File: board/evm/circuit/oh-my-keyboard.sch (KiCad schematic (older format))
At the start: 0 parts

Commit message: evm sch design finished
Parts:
- added P?: CONN_02X12, symbol CONN_02X12
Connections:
- net labels added: +12V, +3.3V, BAT_BST_EN, BAT_DSEL, BAT_IRQ, BAT_OTG_EN, BAT_SCL, BAT_SDA, BAT_nCE, BLE_SCL, BLE_SDA, CDE, CD_SCL, CD_SDA, CHARGEOE, COB1, COB2, DEV_D+, DEV_D-, FSMC_A0, FSMC_A1, FSMC_A2, FSMC_A3, FSMC_A4, FSMC_A5, FSMC_A6, FSMC_A7, FSMC_D0, FSMC_D1, FSMC_D10, FSMC_D11, FSMC_D12, FSMC_D13, FSMC_D14, FSMC_D15, FSMC_D2, FSMC_D3, FSMC_D4, FSMC_D5, FSMC_D6, FSMC_D7, FSMC_D8, FSMC_D9, FSMC_IRQ, FSMC_OE, FSMC_WE, FSMC_nCS, GND, HOST_D+, HOST_D-, LED_Sihft_CLK0, LED_Storage_CLK0, LED_nCLR, LED_nOE, ScanMatrix0, ScanMatrix1, ScanMatrix10, ScanMatrix11, ScanMatrix12, ScanMatrix13, ScanMatrix14, ScanMatrix15, ScanMatrix16, ScanMatrix17, ScanMatrix18, ScanMatrix19, ScanMatrix2, ScanMatrix20, ScanMatrix21, ScanMatrix22, ScanMatrix23, ScanMatrix3, ScanMatrix4, ScanMatrix5, ScanMatrix6, ScanMatrix7, ScanMatrix8, ScanMatrix9, TOUCH_IRQ, TOUCH_SCK, TOUCH_SDA, nRF24_IRQ
- wire segments 0 -> 239
- no-connect marks 0 -> 7

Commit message: add light sensor
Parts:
- added R?: Photores, symbol Photores
- added R?: R62K, symbol R
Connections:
- wire segments 239 -> 245
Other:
- note added: "FIXME: Double check photo resister's light/dark Rval"
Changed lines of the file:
@@
 F64 "GPIO9" I R 6100 6250 60
 F65 "GPIO10" I R 6100 6350 60
+F66 "ADC_IN" I R 6100 6450 60
 $EndSheet
 Wire Wire Line
@@
 Text Label 6200 6050 0    60   ~ 0
 CDE
+$Comp
+L Photores R?
+U 1 1 575DF76C
+P 7800 6900
+F 0 "R?" V 7880 6900 50  0000 C CNN
+F 1 "Photores" V 8010 6900 50  0000 C TNN
+F 2 "" V 7730 6900 50  0000 C CNN
+F 3 "" H 7800 6900 50  0000 C CNN
+	1    7800 6900
+	1    0    0    -1
+$EndComp
+$Comp
+L +3.3V #PWR?
+U 1 1 575E1819
+P 8350 6400
+F 0 "#PWR?" H 8350 6250 50  0001 C CNN
+F 1 "+3.3V" H 8350 6540 50  0000 C CNN
+F 2 "" H 8350 6400 50  0000 C CNN
+F 3 "" H 8350 6400 50  0000 C CNN
+	1    8350 6400
+	1    0    0    -1
+$EndComp
+$Comp
+L R R?
+U 1 1 575E386A
+P 8050 6450
+F 0 "R?" V 8130 6450 50  0000 C CNN
+F 1 "R62K" V 8050 6450 50  0000 C CNN
+F 2 "" V 7980 6450 50  0000 C CNN
+F 3 "" H 8050 6450 50  0000 C CNN
+	1    8050 6450
+	0    1    1    0
+$EndComp
+Wire Wire Line
+	7800 6650 7800 6450
+Wire Wire Line
+	7800 6450 7900 6450
+Wire Wire Line
+	8200 6450 8350 6450
+Wire Wire Line
+	8350 6450 8350 6400
+$Comp
+L GND #PWR?
+U 1 1 575E448B
+P 7800 7250
+F 0 "#PWR?" H 7800 7000 50  0001 C CNN
+F 1 "GND" H 7800 7100 50  0000 C CNN
+F 2 "" H 7800 7250 50  0000 C CNN
+F 3 "" H 7800 7250 50  0000 C CNN
+	1    7800 7250
+	1    0    0    -1
+$EndComp
+Wire Wire Line
+	7800 7250 7800 7150
+Wire Wire Line
+	6100 6450 7800 6450
+Connection ~ 7800 6450
+Text Notes 8200 6700 0    60   ~ 0
+FIXME: Double check photo resister's light/dark Rval
 $EndSCHEMATC

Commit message: bug fix
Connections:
- net labels added: LED_DATA, LED_Sihft_CLK, LED_Storage_CLK
- net labels removed: LED_Sihft_CLK0, LED_Storage_CLK0
- wire segments 245 -> 247
- no-connect marks 7 -> 6

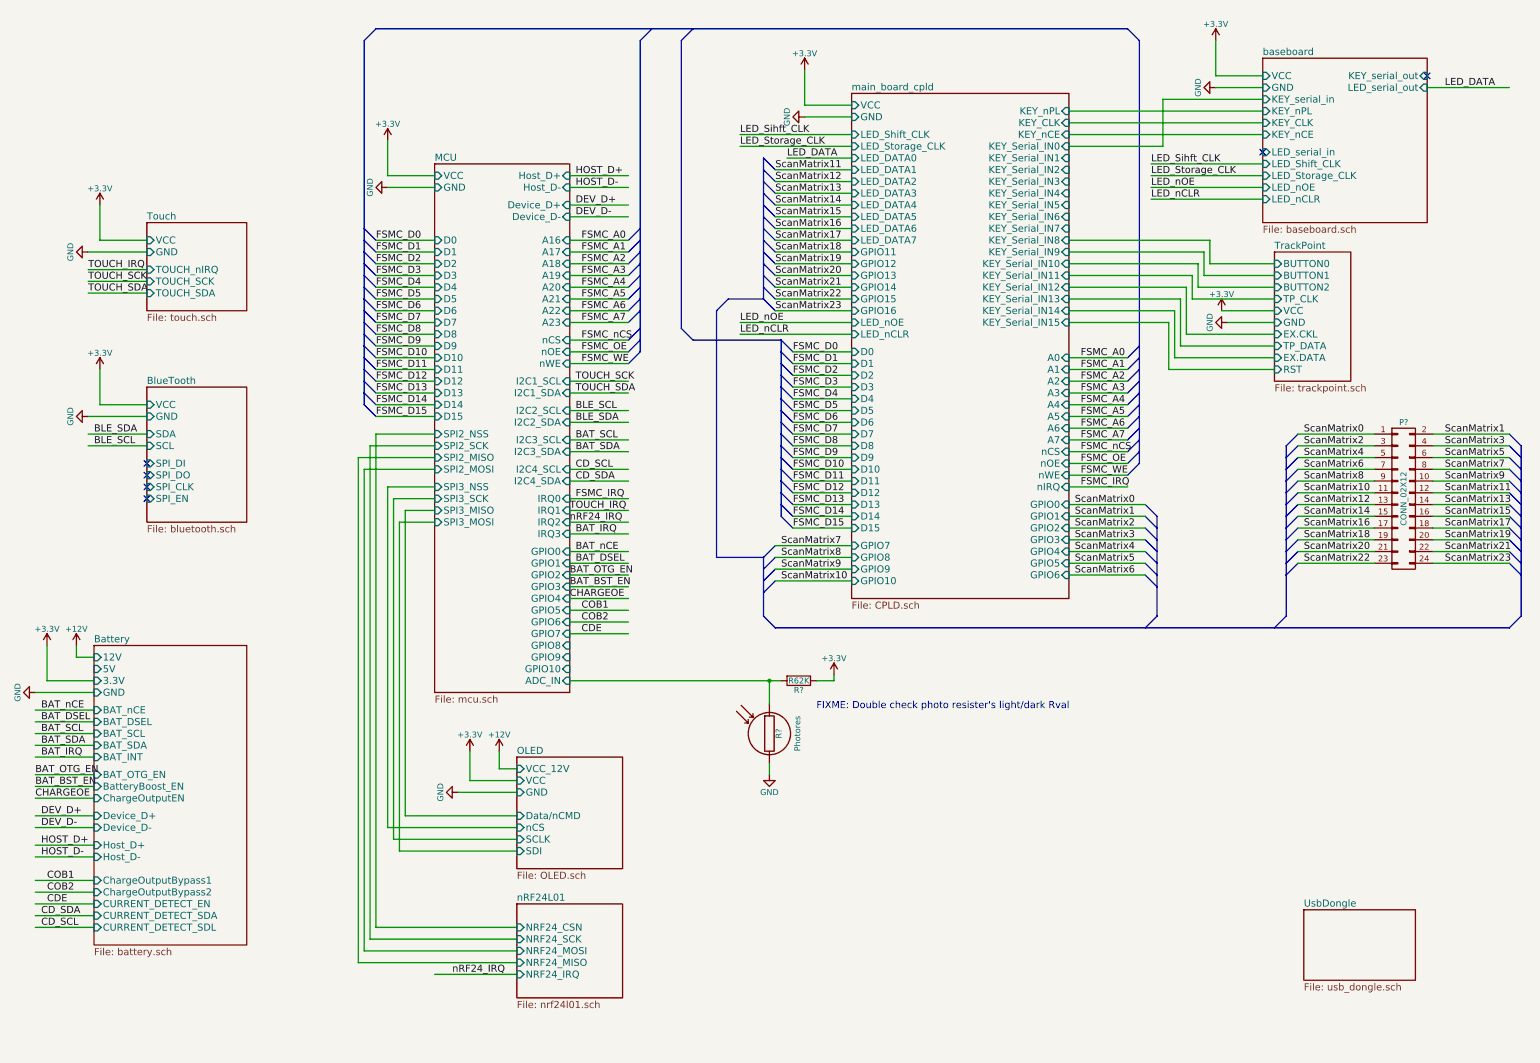
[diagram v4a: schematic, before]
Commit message: set boot0 to 0
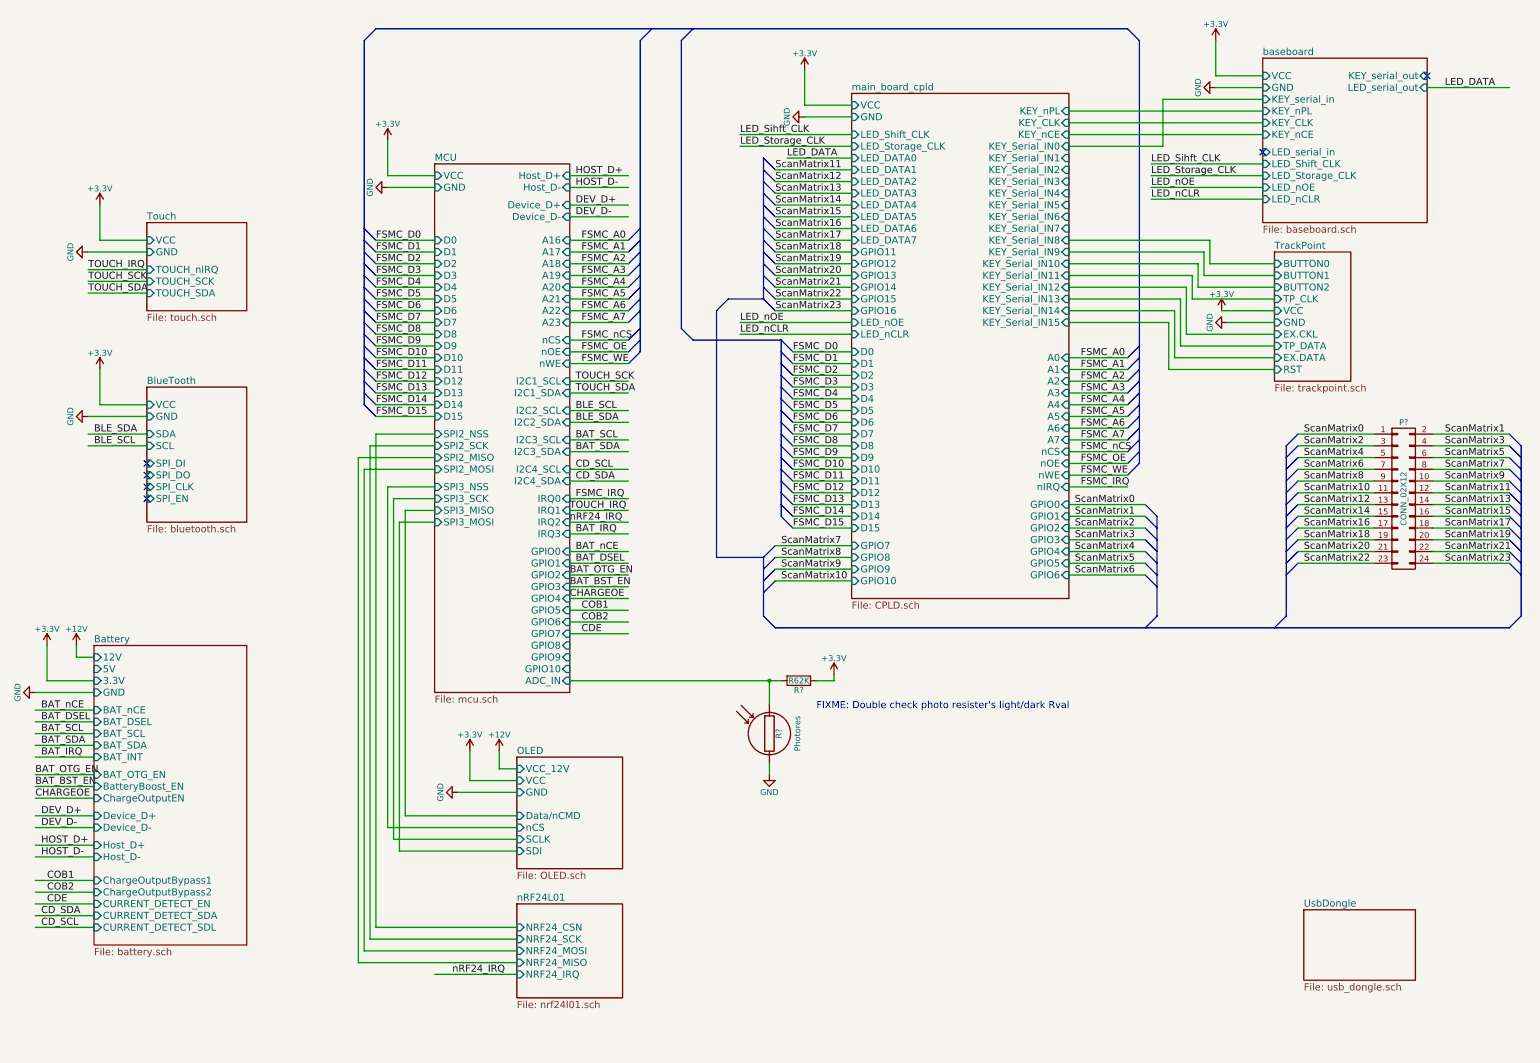
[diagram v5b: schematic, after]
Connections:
- wire segments 247 -> 246
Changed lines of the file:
@@
 	10950 4300 10850 4400
 Wire Bus Line
-	10950 1000 10950 3600
-Wire Bus Line
-	10950 3600 10950 3700
-Wire Bus Line
-	10950 3700 10950 3800
-Wire Bus Line
-	10950 3800 10950 3900
-Wire Bus Line
-	10950 3900 10950 4000
-Wire Bus Line
-	10950 4000 10950 4100
-Wire Bus Line
-	10950 4100 10950 4200
-Wire Bus Line
-	10950 4200 10950 4300
-Wire Bus Line
-	10950 4300 10950 4400
-Wire Bus Line
-	10950 4400 10950 4500
-Wire Bus Line
-	10950 4500 10950 4600
+	10950 1000 10950 4600
 Wire Bus Line
 	10850 900  10950 1000
@@
 	4450 900  10850 900
 Wire Bus Line
-	7900 3550 7900 3650
-Wire Bus Line
-	7900 3650 7900 3750
-Wire Bus Line
-	7900 3750 7900 3850
-Wire Bus Line
-	7900 3850 7900 3950
-Wire Bus Line
-	7900 3950 7900 4050
-Wire Bus Line
-	7900 4050 7900 4150
-Wire Bus Line
-	7900 4150 7900 4250
-Wire Bus Line
-	7900 4250 7900 4350
-Wire Bus Line
-	7900 4350 7900 4450
-Wire Bus Line
-	7900 4450 7900 4550
-Wire Bus Line
-	7900 4550 7900 4650
-Wire Bus Line
-	7900 4650 7900 4750
-Wire Bus Line
-	7900 4750 7900 4850
-Wire Bus Line
-	7900 4850 7900 4950
-Wire Bus Line
-	7900 4950 7900 5050
+	7900 3550 7900 5050
 Wire Bus Line
 	6800 900  6700 1000
 Wire Bus Line
-	6700 1000 6700 2600
-Wire Bus Line
-	6700 2600 6700 2700
-Wire Bus Line
-	6700 2700 6700 2800
-Wire Bus Line
-	6700 2800 6700 2900
-Wire Bus Line
-	6700 2900 6700 3000
-Wire Bus Line
-	6700 3000 6700 3100
-Wire Bus Line
-	6700 3100 6700 3200
-Wire Bus Line
-	6700 3200 6700 3300
-Wire Bus Line
-	6700 3300 6700 3450
-Wire Bus Line
-	6700 3450 6700 3550
-Wire Bus Line
-	6700 3550 6700 3650
+	6700 1000 6700 3650
 Wire Bus Line
 	4450 900  4350 1000
 Wire Bus Line
-	4350 1000 4350 2600
-Wire Bus Line
-	4350 2600 4350 2700
-Wire Bus Line
-	4350 2700 4350 2800
-Wire Bus Line
-	4350 2800 4350 2900
-Wire Bus Line
-	4350 2900 4350 3000
-Wire Bus Line
-	4350 3000 4350 3100
-Wire Bus Line
-	4350 3100 4350 3200
-Wire Bus Line
-	4350 3200 4350 3300
-Wire Bus Line
-	4350 3300 4350 3400
-Wire Bus Line
-	4350 3400 4350 3500
-Wire Bus Line
-	4350 3500 4350 3600
-Wire Bus Line
-	4350 3600 4350 3700
-Wire Bus Line
-	4350 3700 4350 3800
-Wire Bus Line
-	4350 3800 4350 3900
-Wire Bus Line
-	4350 3900 4350 4000
-Wire Bus Line
-	4350 4000 4350 4100
+	4350 1000 4350 4100
 Entry Bus Bus
 	4350 2600 4450 2700
@@
 	7350 5400 7750 5400
 Wire Bus Line
-	7750 5400 7750 5500
-Wire Bus Line
-	7750 5500 7750 5600
-Wire Bus Line
-	7750 5600 7750 5700
-Wire Bus Line
-	7750 5700 7750 5900
+	7750 5400 7750 5900
 Wire Bus Line
 	7750 5900 7850 6000
@@
 	11100 5900 11000 6000
 Wire Bus Line
-	11100 5050 11100 5150
-Wire Bus Line
-	11100 5150 11100 5250
-Wire Bus Line
-	11100 5250 11100 5350
-Wire Bus Line
-	11100 5350 11100 5450
-Wire Bus Line
-	11100 5450 11100 5550
-Wire Bus Line
-	11100 5550 11100 5650
-Wire Bus Line
-	11100 5650 11100 5900
+	11100 5050 11100 5900
 Entry Bus Bus
 	14100 4350 14200 4450
@@
 	12300 5450 12200 5550
 Wire Bus Line
-	12200 4450 12200 4550
-Wire Bus Line
-	12200 4550 12200 4650
-Wire Bus Line
-	12200 4650 12200 4750
-Wire Bus Line
-	12200 4750 12200 4850
-Wire Bus Line
-	12200 4850 12200 4950
-Wire Bus Line
-	12200 4950 12200 5050
-Wire Bus Line
-	12200 5050 12200 5150
-Wire Bus Line
-	12200 5150 12200 5250
-Wire Bus Line
-	12200 5250 12200 5350
-Wire Bus Line
-	12200 5350 12200 5450
-Wire Bus Line
-	12200 5450 12200 5550
-Wire Bus Line
-	12200 5550 12200 5900
+	12200 4450 12200 5900
 Wire Bus Line
 	12200 5900 12100 6000
 Wire Bus Line
-	14200 4450 14200 4550
-Wire Bus Line
-	14200 4550 14200 4650
-Wire Bus Line
-	14200 4650 14200 4750
-Wire Bus Line
-	14200 4750 14200 4850
-Wire Bus Line
-	14200 4850 14200 4950
-Wire Bus Line
-	14200 4950 14200 5050
-Wire Bus Line
-	14200 5050 14200 5150
-Wire Bus Line
-	14200 5150 14200 5250
-Wire Bus Line
-	14200 5250 14200 5350
-Wire Bus Line
-	14200 5350 14200 5450
-Wire Bus Line
-	14200 5450 14200 5550
-Wire Bus Line
-	14200 5550 14200 5900
+	14200 4450 14200 5900
 Wire Bus Line
 	14200 5900 14100 6000
@@
 	7800 6650 7800 6450
 Wire Wire Line
-	6100 6450 7800 6450
-Wire Wire Line
-	7800 6450 7900 6450
+	6100 6450 7900 6450
 Wire Wire Line
 	8200 6450 8350 6450
@@
 	7750 2000 7850 2100
 Wire Bus Line
-	7750 2000 7750 2100
-Wire Bus Line
-	7750 2100 7750 2200
-Wire Bus Line
-	7750 2200 7750 2300
-Wire Bus Line
-	7750 2300 7750 2400
-Wire Bus Line
-	7750 2400 7750 2500
-Wire Bus Line
-	7750 2500 7750 2600
-Wire Bus Line
-	7750 2600 7750 2700
-Wire Bus Line
-	7750 2700 7750 2800
-Wire Bus Line
-	7750 2800 7750 2900
-Wire Bus Line
-	7750 2900 7750 3000
-Wire Bus Line
-	7750 3000 7750 3100
-Wire Bus Line
-	7750 3100 7750 3200
+	7750 2000 7750 3200
 Wire Bus Line
 	7750 3200 7450 3200

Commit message: minor updates
- add lots of test points
- export usart1
- bug fix
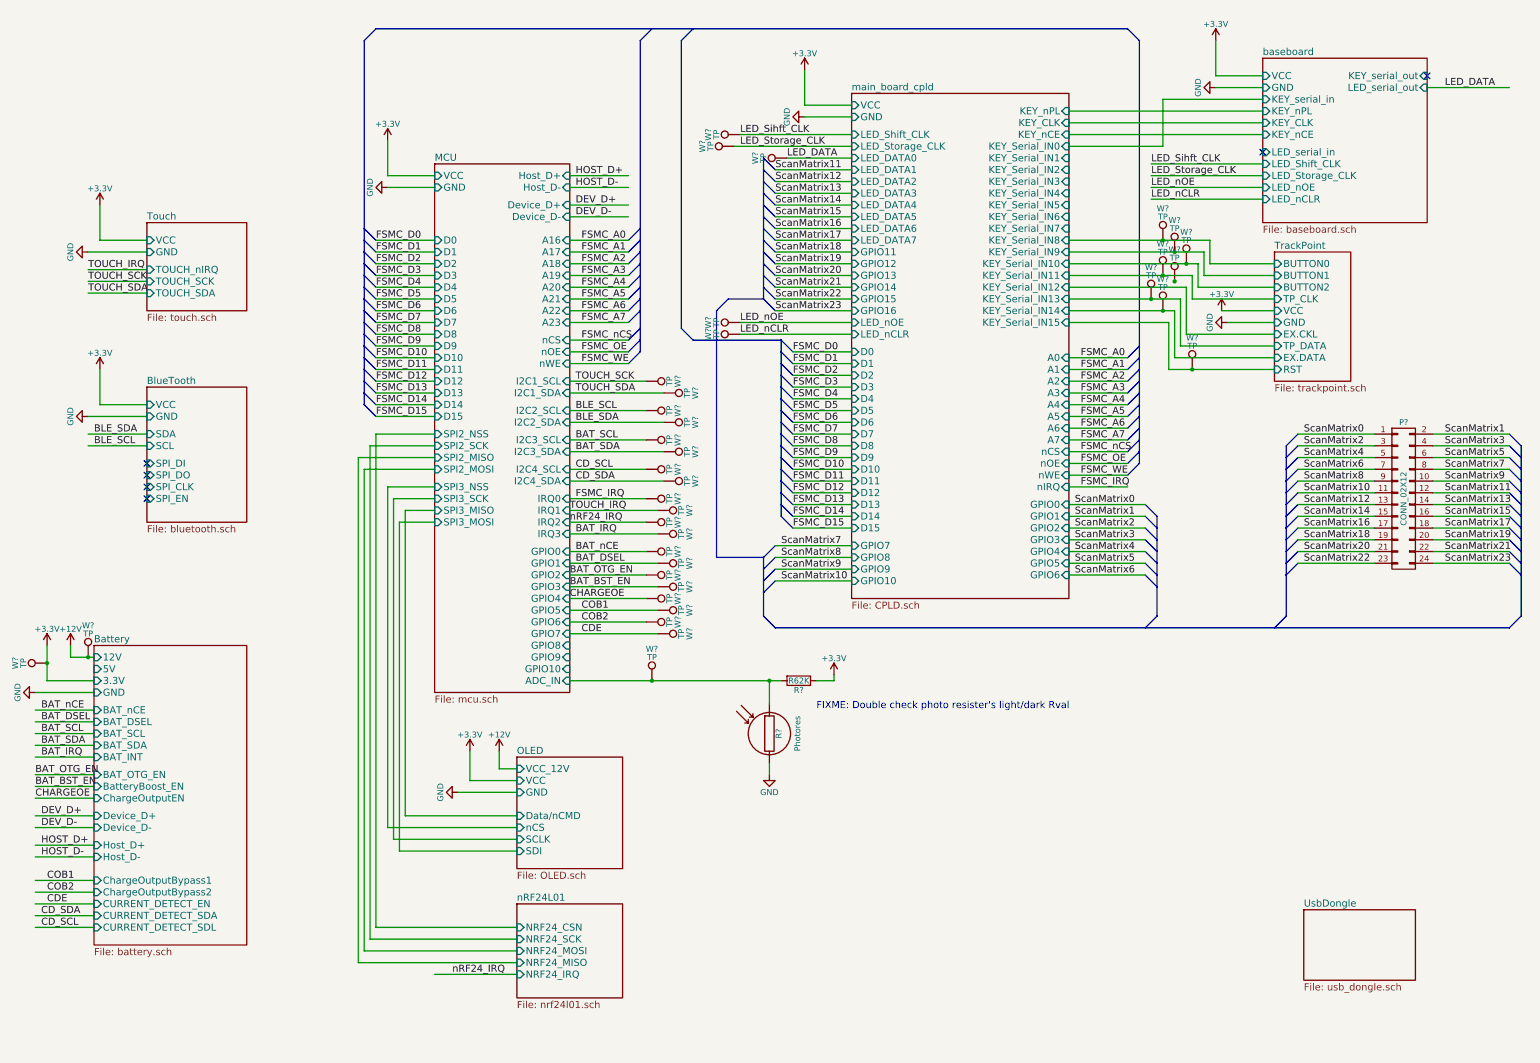
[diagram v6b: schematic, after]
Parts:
- added W? (x36): TP, symbol TEST_1P
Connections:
- wire segments 246 -> 255

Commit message: change cpld to fpga due to limited resource
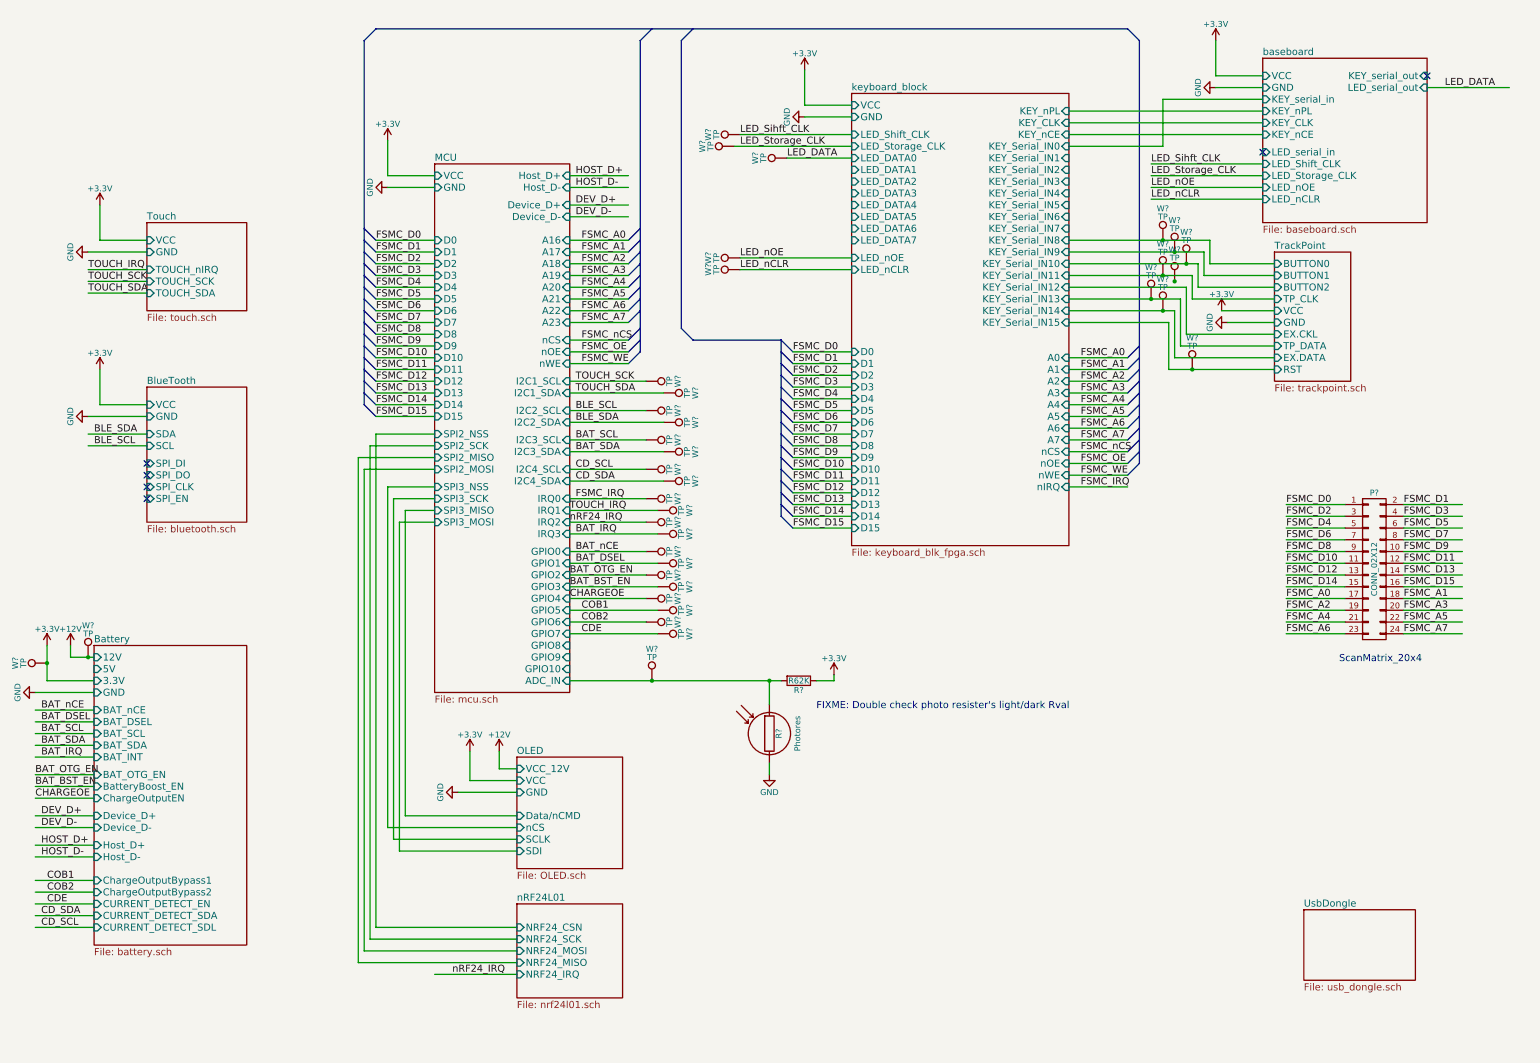
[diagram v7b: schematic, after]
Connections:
- net labels removed: ScanMatrix0, ScanMatrix1, ScanMatrix10, ScanMatrix11, ScanMatrix12, ScanMatrix13, ScanMatrix14, ScanMatrix15, ScanMatrix16, ScanMatrix17, ScanMatrix18, ScanMatrix19, ScanMatrix2, ScanMatrix20, ScanMatrix21, ScanMatrix22, ScanMatrix23, ScanMatrix3, ScanMatrix4, ScanMatrix5, ScanMatrix6, ScanMatrix7, ScanMatrix8, ScanMatrix9
- wire segments 255 -> 222
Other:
- note added: "ScanMatrix_20x4\n"
- moved on the sheet: P?, W?
